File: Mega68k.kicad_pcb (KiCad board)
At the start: 2 copper layers, 101.9 x 53.6 mm, 16 parts, among them J1 CLK Select, J2 Ext CLK, J3 SPI, U1 68000D, U2 AS6C4008-55PCN, U3 AS6C4008-55PCN, X1 CXO_DIP8

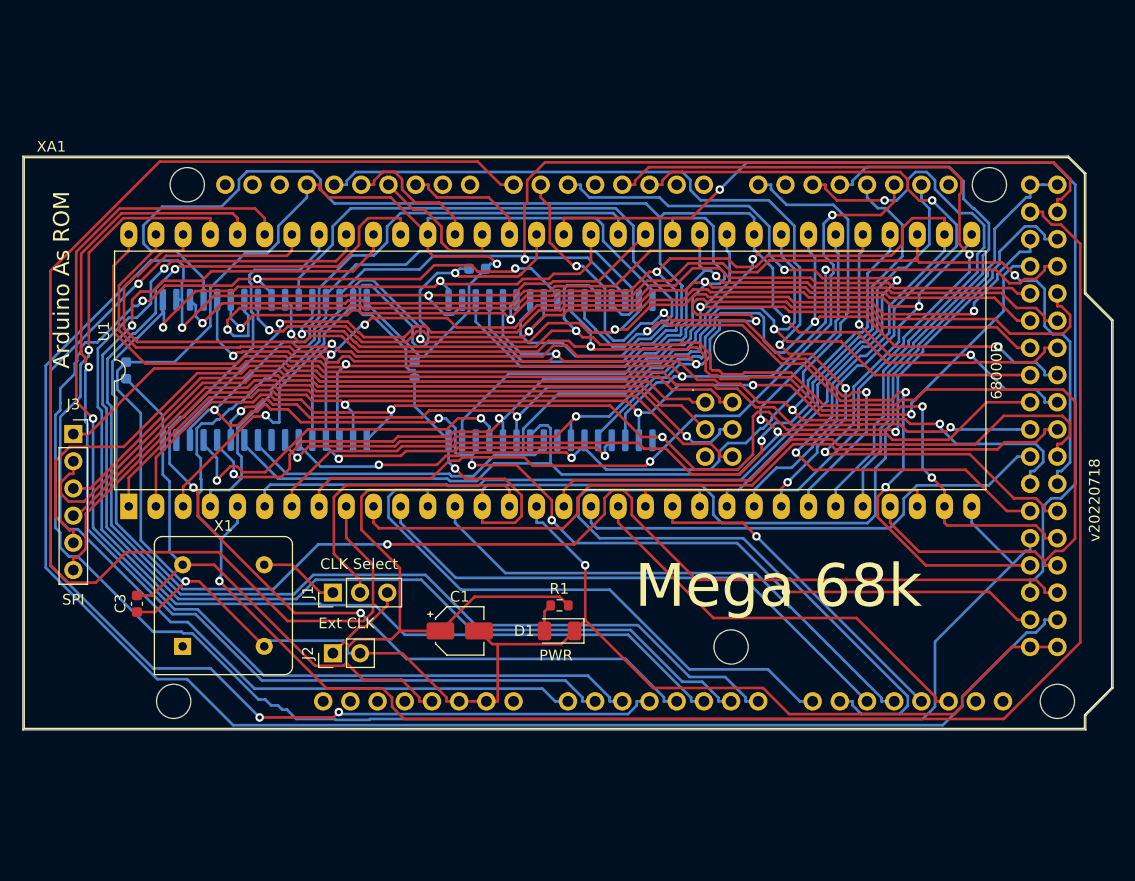
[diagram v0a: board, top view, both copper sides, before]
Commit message: Fixed 64 pin socket size and added more status lights
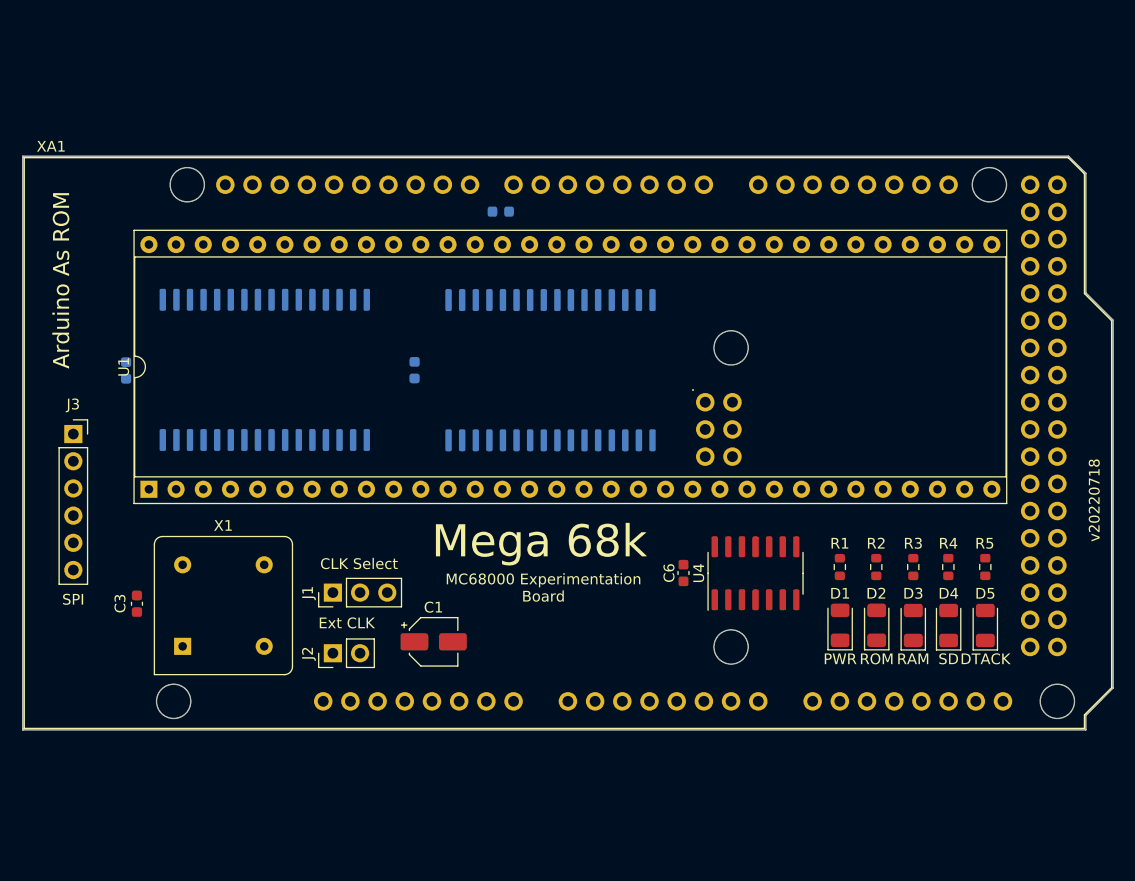
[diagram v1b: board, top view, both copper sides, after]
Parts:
- added C6: .1uF, Capacitor_SMD:C_0603_1608Metric, F.Cu at (109.8, 97.0)
- added D2: ROM, LED_SMD:LED_1206_3216Metric, F.Cu at (127.9, 101.8)
- added D3: RAM, LED_SMD:LED_1206_3216Metric, F.Cu at (131.3, 101.9)
- added D4: SD, LED_SMD:LED_1206_3216Metric, F.Cu at (134.6, 101.9)
- added D5: DTACK, LED_SMD:LED_1206_3216Metric, F.Cu at (138.0, 101.9)
- added R2: 220, Resistor_SMD:R_0603_1608Metric, F.Cu at (127.8, 96.4)
- added R3: 220, Resistor_SMD:R_0603_1608Metric, F.Cu at (131.3, 96.4)
- added R4: 220, Resistor_SMD:R_0603_1608Metric, F.Cu at (134.5, 96.4)
- added R5: 220, Resistor_SMD:R_0603_1608Metric, F.Cu at (138.0, 96.4)
- added U4: 74HC14, Package_SO:SOIC-14_3.9x8.7mm_P1.27mm, F.Cu at (116.5, 97.0)
- U1: footprint Package_DIP:DIP-64_W25.4mm_LongPads -> Package_DIP:DIP-64_W22.86mm_Socket
- moved R1 26.4 mm to (124.4, 96.4), turned to -90 degrees
- moved D1 26.2 mm to (124.4, 101.8), turned to 90 degrees
- moved C2 5.76 mm to (92.7, 63.2)
- moved C1 2.64 mm to (86.5, 103.4)
- moved U1 2.47 mm to (59.9, 89.1)
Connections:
- XA1 pad D38: /SDCARD_SEL -> /~{SDCARD_SEL}
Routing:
- net VCC: track 253.5 -> 0.00 mm, vias 2 -> 0
- net GND: track 241.5 -> 0.00 mm, vias 3 -> 0
- net /D0: track 207.6 -> 0.00 mm, vias 1 -> 0
- net /A17: track 199.6 -> 0.00 mm, vias 2 -> 0
- net /A4: track 187.5 -> 0.00 mm, vias 3 -> 0
- net /A19: track 172.5 -> 0.00 mm, vias 3 -> 0
- net /A6: track 157.1 -> 0.00 mm, vias 3 -> 0
- net /D7: track 146.9 -> 0.00 mm, vias 3 -> 0
- net /A13: track 145.9 -> 0.00 mm, vias 1 -> 0
- net /A18: track 144.9 -> 0.00 mm, vias 5 -> 0
- net /D6: track 139.5 -> 0.00 mm, vias 4 -> 0
- net /A16: track 134.6 -> 0.00 mm, vias 2 -> 0
- net /A1: track 126.4 -> 0.00 mm, vias 2 -> 0
- net /D5: track 125.5 -> 0.00 mm, vias 3 -> 0
- net /A15: track 123.4 -> 0.00 mm, vias 2 -> 0
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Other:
- board text added: "MC68000 Experimentation Board"

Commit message: Updated version label
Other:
- board text added: "v20220804"
- board text removed: "v20220718"
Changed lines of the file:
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@@
     (effects (font (size 1 1) (thickness 0.25)))
   )
-  (gr_text "v20220718" (at 148.209 90.1446 90) (layer "F.SilkS")
+  (gr_text "v20220804" (at 148.209 90.1446 90) (layer "F.SilkS")
     (effects (font (size 1 1) (thickness 0.2)))
   )

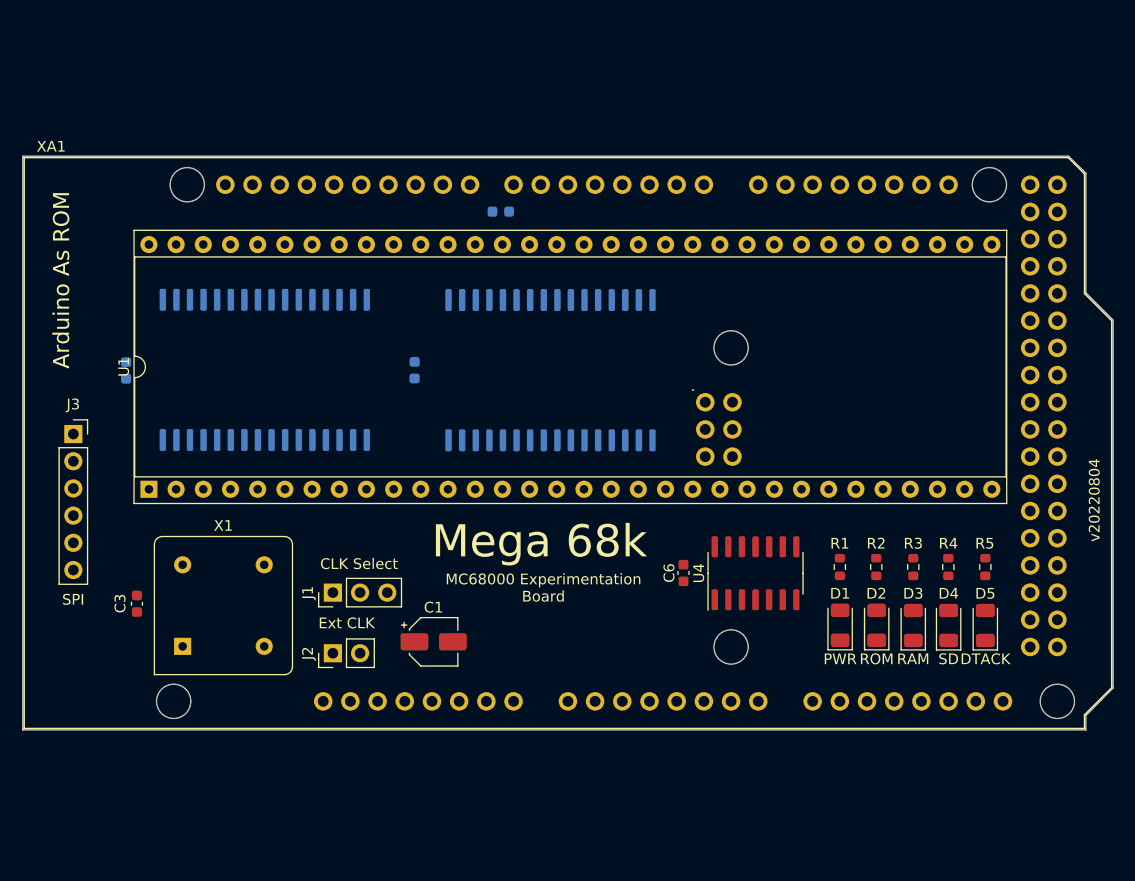
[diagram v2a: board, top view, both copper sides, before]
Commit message: Updated with trace routing
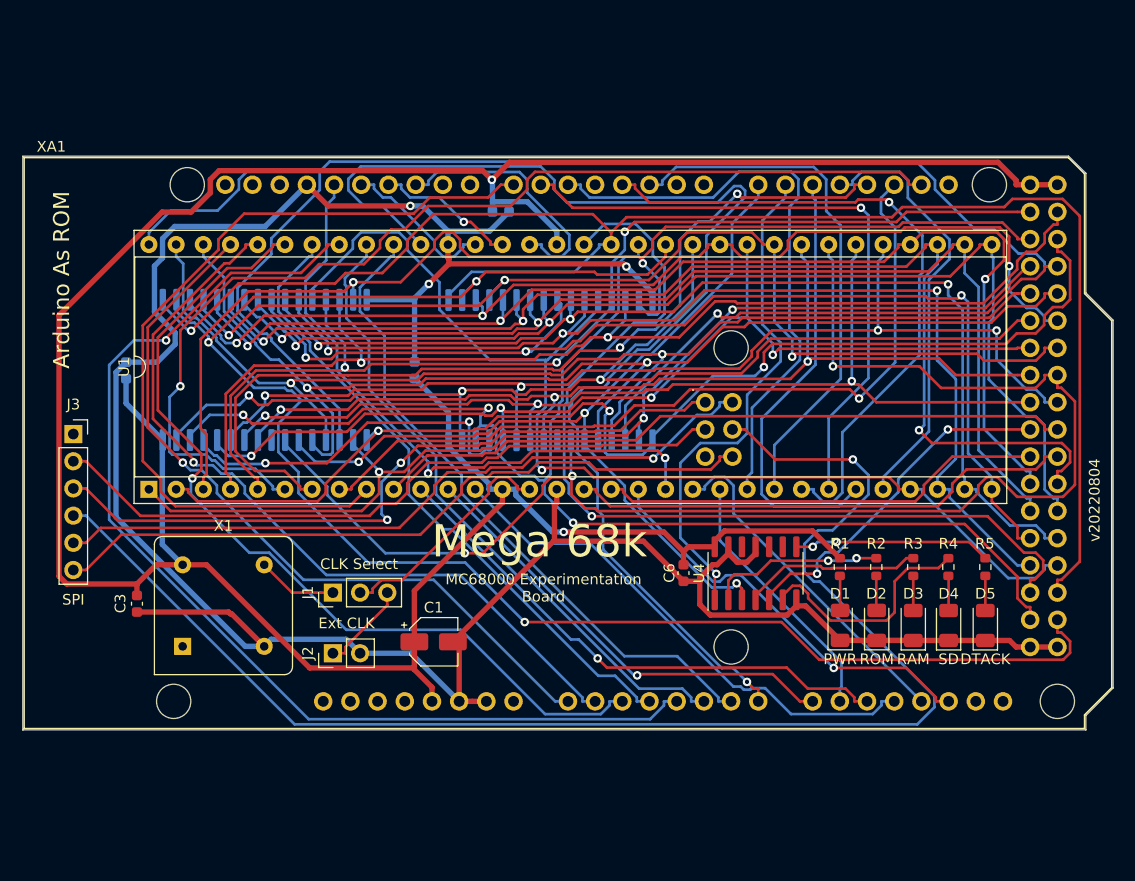
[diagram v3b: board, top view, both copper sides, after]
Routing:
- net VCC: track 0.00 -> 272.7 mm, vias 0 -> 2
- net GND: track 0.00 -> 248.7 mm, vias 0 -> 3
- net /D5: track 0.00 -> 176.1 mm, vias 0 -> 1
- net /A17: track 0.00 -> 159.1 mm, vias 0 -> 3
- net /A19: track 0.00 -> 149.9 mm, vias 0 -> 1
- net /A11: track 0.00 -> 136.2 mm, vias 0 -> 3
- net /SPI_MISO: track 0.00 -> 134.0 mm, vias 0 -> 1
- net /A18: track 0.00 -> 122.7 mm, vias 0 -> 3
- net /D15: track 0.00 -> 114.7 mm, vias 0 -> 1
- net /A7: track 0.00 -> 111.8 mm, vias 0 -> 3
- net /D7: track 0.00 -> 110.9 mm, vias 0 -> 2
- net /D2: track 0.00 -> 110.6 mm, vias 0 -> 2
- net /D3: track 0.00 -> 108.9 mm, vias 0 -> 3
- net /D6: track 0.00 -> 108.8 mm, vias 0 -> 2
- net /A8: track 0.00 -> 108.6 mm, vias 0 -> 3
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
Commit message: Added an arduino reset switch
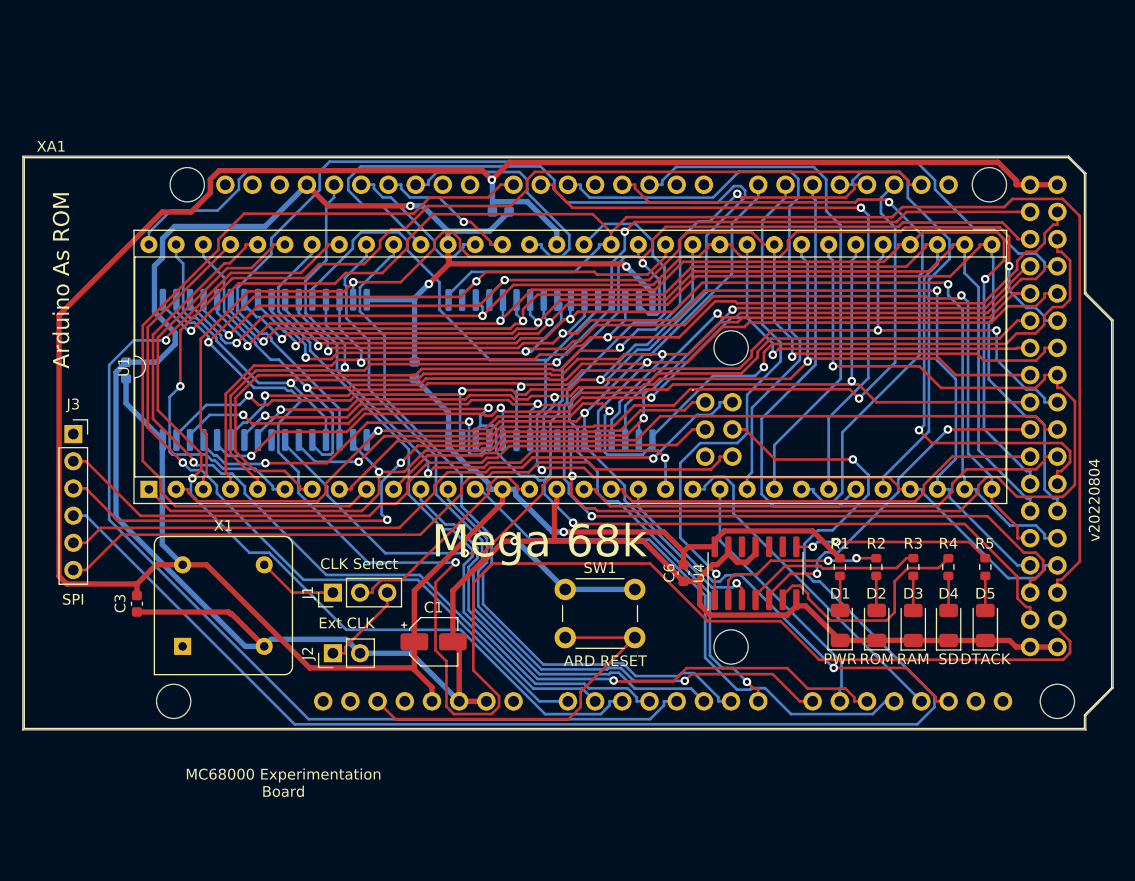
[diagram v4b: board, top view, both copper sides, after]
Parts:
- added SW1: ARD RESET, Button_Switch_THT:SW_PUSH_6mm, F.Cu at (98.8, 98.5)
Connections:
- XA1 pad RST1: unconnected-(XA1-PadRST1) -> /~{ARD_RESET}
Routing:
- net /~{ARD_RESET}: track 0.00 -> 35.2 mm
- net /A17: track 159.1 -> 190.7 mm
- net GND: track 248.7 -> 264.5 mm, vias 3 -> 4
- net /BG: track 50.1 -> 56.3 mm
- net /BGACK: track 42.4 -> 48.3 mm
- net /D14: track 62.1 -> 68.0 mm
- net /D13: track 60.9 -> 65.7 mm
- net /D11: track 60.6 -> 65.0 mm
- net /BR: track 48.7 -> 52.0 mm
- net /D15: track 114.7 -> 115.2 mm

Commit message: Added freerun software sketch for platformio
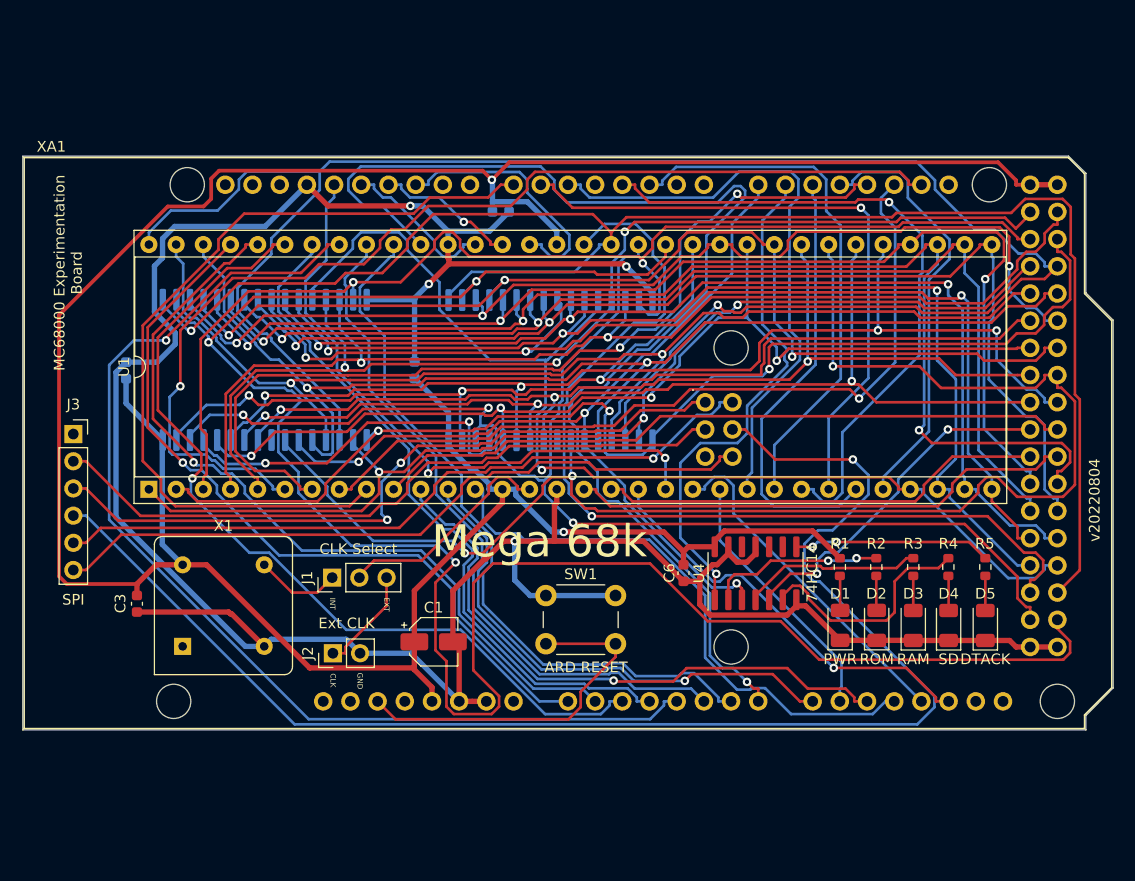
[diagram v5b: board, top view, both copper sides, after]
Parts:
- moved SW1 1.89 mm to (97.0, 99.1)
- moved J1 1.40 mm to (77.0, 97.4)
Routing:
- net /BR: track 52.0 -> 53.6 mm
- net /D9: track 74.1 -> 75.5 mm
- net /EXT_CLK: track 8.46 -> 9.83 mm
- net /D8: track 70.6 -> 71.9 mm
- net /~{ARD_RESET}: track 35.2 -> 33.9 mm
- net /A14: track 94.9 -> 96.2 mm
- net /A16: track 107.6 -> 108.8 mm
- net /D5: track 176.1 -> 177.1 mm
- net /D4: track 101.4 -> 102.3 mm
- net /D0: track 102.5 -> 103.4 mm
- net /D6: track 108.8 -> 109.6 mm
- net /~{ROM_SEL}: track 47.8 -> 48.5 mm
- net /A9: track 100.8 -> 101.5 mm
- net /CPU_CLK: track 21.6 -> 21.0 mm
- net GND: track 264.5 -> 265.1 mm
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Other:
- board text added: "CLK"
- board text added: "EXT"
- board text added: "GND"
- board text added: "INT"
- board text removed: "Arduino As ROM"

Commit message: Working freerun
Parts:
- removed C4, C5: .1uF, Capacitor_SMD:C_0603_1608Metric
- removed U2, U3: AS6C4008-55PCN, Package_SO:SSOP-32_11.305x20.495mm_P1.27mm
- added C7: .1uF, Capacitor_SMD:C_0603_1608Metric, B.Cu at (95.6, 86.9)
- added J4: Debug, Connector_PinHeader_2.54mm:PinHeader_2x34_P2.54mm_Vertical, F.Cu at (59.2, 118.6)
- added J4: Debug, Connector_PinHeader_2.54mm:PinHeader_2x34_P2.54mm_Vertical, F.Cu at (59.2, 54.2)
- added R6: 10k, Resistor_SMD:R_0603_1608Metric, F.Cu at (113.8, 99.6)
- added SW2: CPU_RESET, Button_Switch_THT:SW_PUSH_6mm, F.Cu at (103.5, 99.6)
- moved C6 10.8 mm to (120.2, 94.0), turned to 180 degrees
- moved C2 5.51 mm to (92.8, 68.7)
- moved U4 5.28 mm to (120.2, 100.8), turned to 0 degrees
- moved SW1 4.43 mm to (92.6, 99.6)
- moved J3 2.64 mm to (55.1, 82.8)
- moved R2 1.83 mm to (129.1, 97.7)
- moved D1 1.83 mm to (125.7, 103.1)
- moved D2 1.83 mm to (129.1, 103.1)
- moved D3 1.83 mm to (132.6, 103.1)
- moved D4 1.83 mm to (135.9, 103.1)
- moved D5 1.83 mm to (139.3, 103.1)
- moved R1 1.83 mm to (125.7, 97.7)
- moved R3 1.83 mm to (132.6, 97.7)
- moved R4 1.83 mm to (135.8, 97.7)
- moved R5 1.83 mm to (139.3, 97.7)
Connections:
- XA1 pad D21: unconnected-(XA1-PadD21) -> /INT_CLK
- XA1 pad D4: unconnected-(XA1-PadD4) -> /CPU_RST
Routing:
- net VCC: track 273.0 -> 0.00 mm, vias 2 -> 0
- net GND: track 265.1 -> 0.00 mm, vias 4 -> 0
- net /A17: track 190.7 -> 0.00 mm, vias 3 -> 0
- net /D5: track 177.1 -> 0.00 mm, vias 1 -> 0
- net /A19: track 149.7 -> 0.00 mm, vias 1 -> 0
- net /A11: track 136.2 -> 0.00 mm, vias 3 -> 0
- net /SPI_MISO: track 134.0 -> 0.00 mm, vias 1 -> 0
- net /A18: track 122.7 -> 0.00 mm, vias 3 -> 0
- net /D15: track 115.2 -> 0.00 mm, vias 1 -> 0
- net /A7: track 111.8 -> 0.00 mm, vias 3 -> 0
- net /D7: track 110.9 -> 0.00 mm, vias 2 -> 0
- net /D2: track 110.6 -> 0.00 mm, vias 2 -> 0
- net /D6: track 109.6 -> 0.00 mm, vias 2 -> 0
- net /D3: track 109.3 -> 0.00 mm, vias 3 -> 0
- net /A16: track 108.8 -> 0.00 mm, vias 3 -> 0
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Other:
- board size 101.9 x 53.6 mm -> 98.1 x 75.5 mm
- board text added: "v20220807"
- board text removed: "v20220804"
